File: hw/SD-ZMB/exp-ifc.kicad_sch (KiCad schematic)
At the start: 77 parts, among them J10 HDR 1x04 Socket, J12 SOCKET 02x40 (BRD-CONN), J14 HDR 1x04 Socket, J16 HDR 1x3 Pin, J17 HDR 2x10 Pin, J18 DE9 Male (PINS), J3 HDR 1x02 Pin, J4 BARREL JACK, J8 HDR 02x20 PIN (Ribbon Socket), J9 HDR 02x20 PIN (Ribbon Socket), M1 AES-FTDI_FT234XF_USB_UART_Mod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, M2 DISPLAY, Q1 DMG2305UX, SW2 SW Toggle PCB, U31 3.6864MHz Can Osc, U33 Z84C30 CTC, U34 74ACT10, U35 Z84C42 SIO/2, U36 SN74LVC8T245NS, U37 74AHCT1G02, U39 74AHCT04, U4 74AHCT08, U43 74LVC125AS, U45 WS-RP2040-Zero, U46 MAX232/ST232, U47 74LVC1G06W, U5 74AHCT08

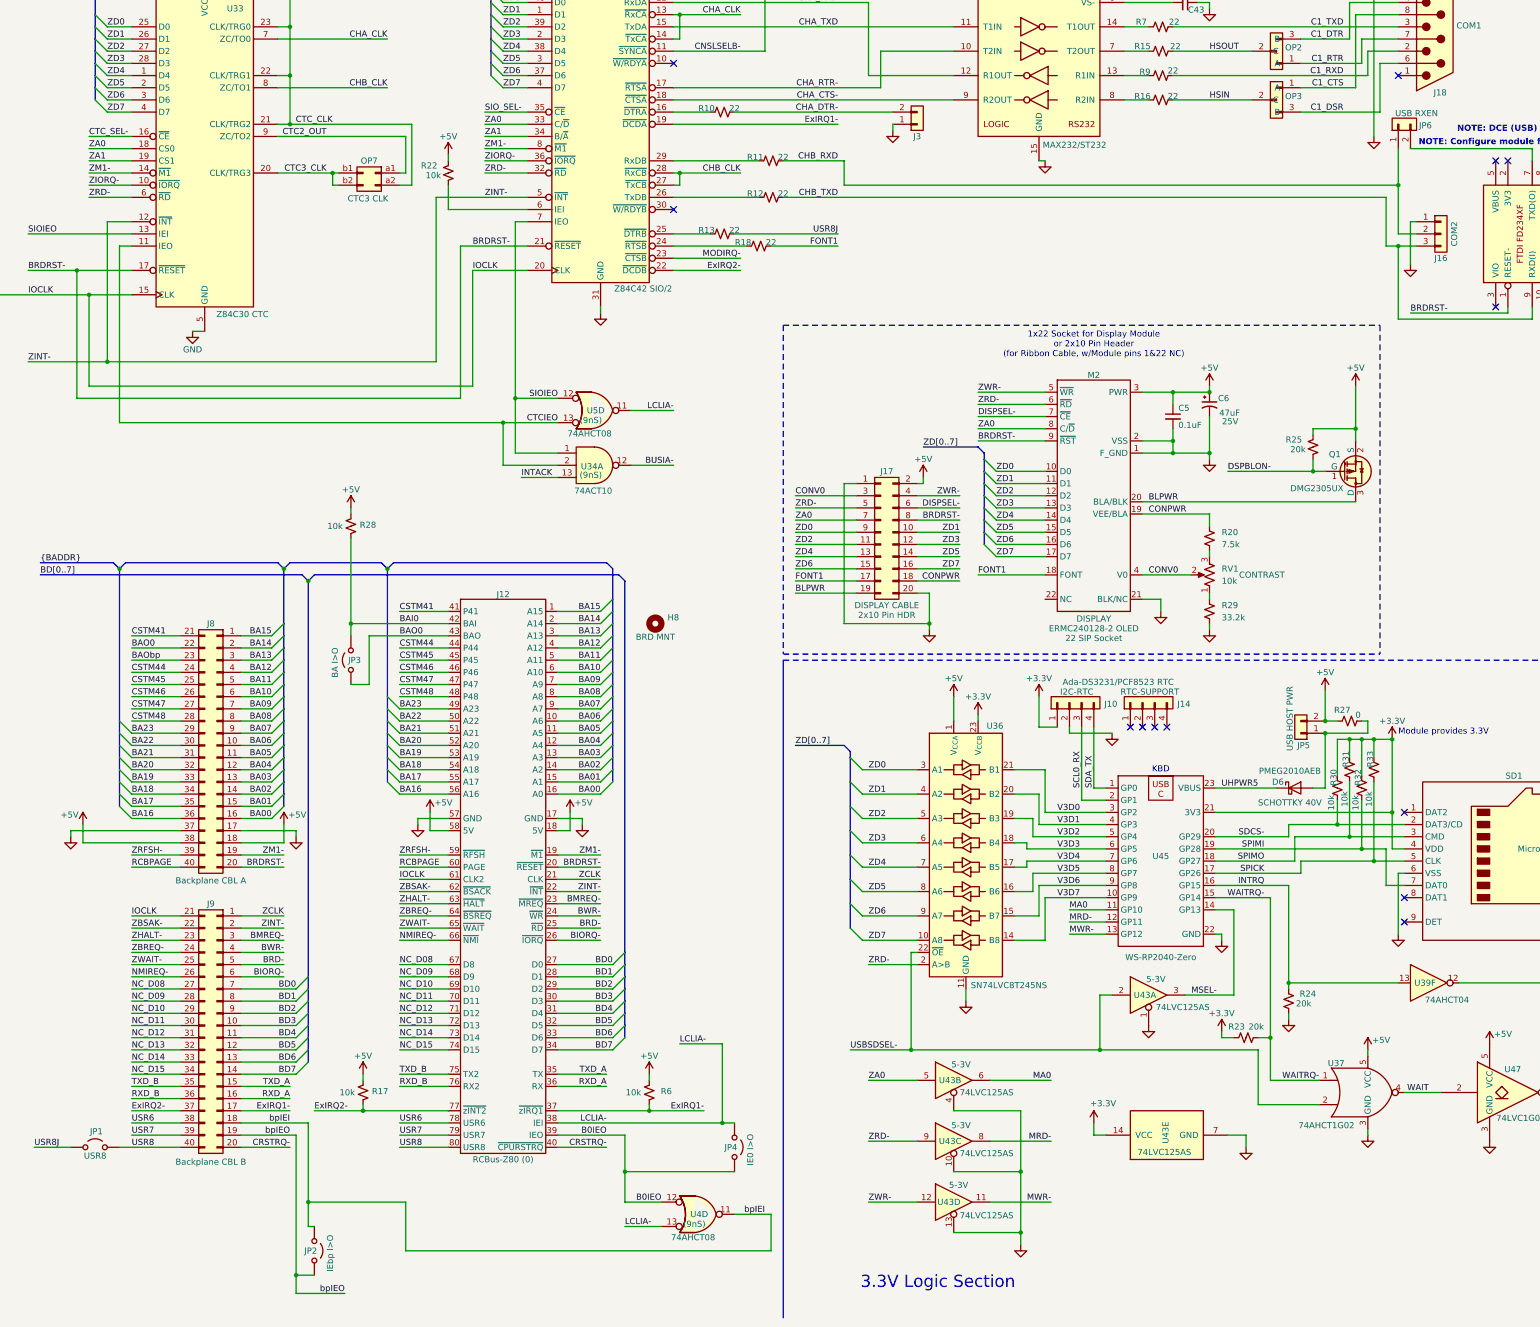
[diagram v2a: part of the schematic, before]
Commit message: ZMB gerbers created. OLED display portion updates.
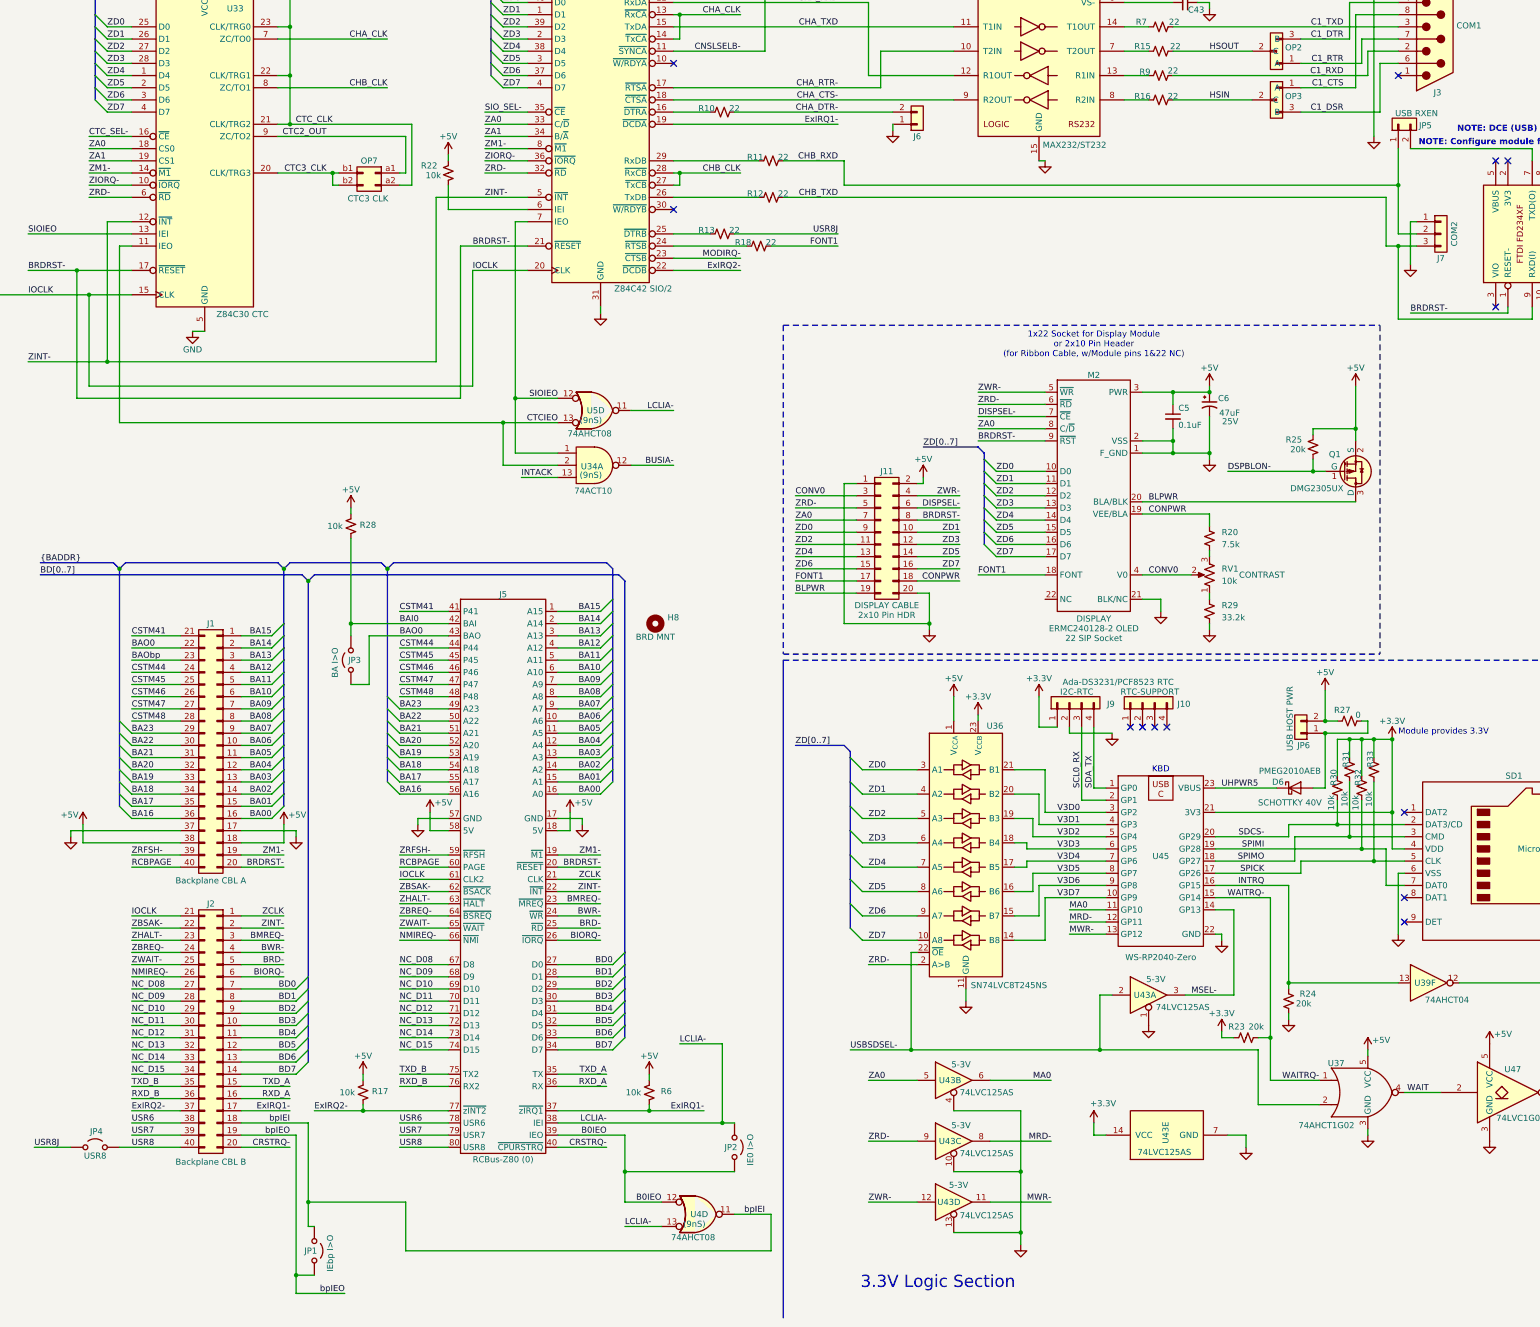
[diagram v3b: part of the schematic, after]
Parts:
- renumbered J8 to J1, J14 to J10, J17 to J11, J9 to J2, J18 to J3, J12 to J5, J3 to J6, J16 to J7, J10 to J9, JP2 to JP1, JP4 to JP2, JP1 to JP4, JP6 to JP5, JP5 to JP6
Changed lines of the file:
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@@
 		(on_board yes)
 		(dnp no)
-		(property "Reference" "JP1"
+		(property "Reference" "JP4"
 			(at 90.424 272.288 0)
 			(effects
@@
 			(project ""
 				(path "/62236e9f-ef27-467c-852b-587c32c473f1/c744ff77-26bb-4e1e-8dbf-a9eea5814d68"
-					(reference "JP1")
+					(reference "JP4")
 					(unit 1)
 				)
@@
 		(on_board yes)
 		(dnp no)
-		(property "Reference" "J8"
+		(property "Reference" "J1"
 			(at 114.3 166.37 0)
 			(effects
@@
 			(project ""
 				(path "/62236e9f-ef27-467c-852b-587c32c473f1/c744ff77-26bb-4e1e-8dbf-a9eea5814d68"
-					(reference "J8")
+					(reference "J1")
 					(unit 1)
 				)
@@
 		(on_board yes)
 		(dnp no)
-		(property "Reference" "J16"
+		(property "Reference" "J7"
 			(at 370.84 90.17 0)
 			(effects
@@
 			(project "SD-ZMB"
 				(path "/62236e9f-ef27-467c-852b-587c32c473f1/c744ff77-26bb-4e1e-8dbf-a9eea5814d68"
-					(reference "J16")
+					(reference "J7")
 					(unit 1)
 				)
@@
 		(on_board yes)
 		(dnp no)
-		(property "Reference" "J14"
+		(property "Reference" "J10"
 			(at 317.246 183.134 90)
 			(effects
@@
 			(project "SD-ZMB"
 				(path "/62236e9f-ef27-467c-852b-587c32c473f1/c744ff77-26bb-4e1e-8dbf-a9eea5814d68"
-					(reference "J14")
+					(reference "J10")
 					(unit 1)
 				)
@@
 		(on_board yes)
 		(dnp no)
-		(property "Reference" "JP6"
+		(property "Reference" "JP5"
 			(at 366.268 62.484 90)
 			(effects
@@
 			(project "SD-ZMB"
 				(path "/62236e9f-ef27-467c-852b-587c32c473f1/c744ff77-26bb-4e1e-8dbf-a9eea5814d68"
-					(reference "JP6")
+					(reference "JP5")
 					(unit 1)
 				)
@@
 		(on_board yes)
 		(dnp no)
-		(property "Reference" "J18"
+		(property "Reference" "J3"
 			(at 369.316 55.626 0)
 			(effects
@@
 			(project ""
 				(path "/62236e9f-ef27-467c-852b-587c32c473f1/c744ff77-26bb-4e1e-8dbf-a9eea5814d68"
-					(reference "J18")
+					(reference "J3")
 					(unit 1)
 				)
@@
 		(on_board yes)
 		(dnp no)
-		(property "Reference" "JP5"
+		(property "Reference" "JP6"
 			(at 340.868 191.77 0)
 			(effects
@@
 			(project "SD-ZMB"
 				(path "/62236e9f-ef27-467c-852b-587c32c473f1/c744ff77-26bb-4e1e-8dbf-a9eea5814d68"
-					(reference "JP5")
+					(reference "JP6")
 					(unit 1)
 				)
@@
 		(on_board yes)
 		(dnp no)
-		(property "Reference" "J10"
+		(property "Reference" "J9"
 			(at 302.006 183.134 90)
 			(effects
@@
 			(project "SD-ZMB"
 				(path "/62236e9f-ef27-467c-852b-587c32c473f1/c744ff77-26bb-4e1e-8dbf-a9eea5814d68"
-					(reference "J10")
+					(reference "J9")
 					(unit 1)
 				)
@@
 		(on_board yes)
 		(dnp no)
-		(property "Reference" "JP2"
+		(property "Reference" "JP1"
 			(at 135.128 297.18 90)
 			(effects
@@
 			(project "SD-ZMB"
 				(path "/62236e9f-ef27-467c-852b-587c32c473f1/c744ff77-26bb-4e1e-8dbf-a9eea5814d68"
-					(reference "JP2")
+					(reference "JP1")
 					(unit 1)
 				)
@@
 		(on_board yes)
 		(dnp no)
-		(property "Reference" "JP4"
+		(property "Reference" "JP2"
 			(at 222.758 275.59 90)
 			(effects
@@
 			(project "SD-ZMB"
 				(path "/62236e9f-ef27-467c-852b-587c32c473f1/c744ff77-26bb-4e1e-8dbf-a9eea5814d68"
-					(reference "JP4")
+					(reference "JP2")
 					(unit 1)
 				)
@@
 		(on_board yes)
 		(dnp no)
-		(property "Reference" "J12"
+		(property "Reference" "J5"
 			(at 175.26 160.274 0)
 			(effects
@@
 			(project ""
 				(path "/62236e9f-ef27-467c-852b-587c32c473f1/c744ff77-26bb-4e1e-8dbf-a9eea5814d68"
-					(reference "J12")
+					(reference "J5")
 					(unit 1)
 				)
@@
 		(on_board yes)
 		(dnp no)
-		(property "Reference" "J3"
+		(property "Reference" "J6"
 			(at 261.62 64.77 0)
 			(effects
@@
 			(project ""
 				(path "/62236e9f-ef27-467c-852b-587c32c473f1/c744ff77-26bb-4e1e-8dbf-a9eea5814d68"
-					(reference "J3")
+					(reference "J6")
 					(unit 1)
 				)
@@
 		(on_board yes)
 		(dnp no)
-		(property "Reference" "J9"
+		(property "Reference" "J2"
 			(at 114.3 224.79 0)
 			(effects
@@
 			(project "SD-ZMB"
 				(path "/62236e9f-ef27-467c-852b-587c32c473f1/c744ff77-26bb-4e1e-8dbf-a9eea5814d68"
-					(reference "J9")
+					(reference "J2")
 					(unit 1)
 				)
@@
 		(on_board yes)
 		(dnp no)
-		(property "Reference" "J17"
+		(property "Reference" "J11"
 			(at 255.27 134.62 0)
 			(effects
@@
 			(project ""
 				(path "/62236e9f-ef27-467c-852b-587c32c473f1/c744ff77-26bb-4e1e-8dbf-a9eea5814d68"
-					(reference "J17")
+					(reference "J11")
 					(unit 1)
 				)

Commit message: PCB received
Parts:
- M2: renamed from U45; Function (none) -> USB KBD
- renumbered C39 to C44, C38 to C45, C44 to C46, M2 to DISP1, U31 to U1, U5 to U15, U4 to U17, U35 to U22, U33 to U26, U47 to U33, U43 to U37, U39 to U41, U37 to U43, U34 to U7, U46 to U8
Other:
- note removed: "KBD"
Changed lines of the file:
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@@
 		)
 	)
-	(text "KBD"
-		(exclude_from_sim no)
-		(at 312.42 196.85 0)
-		(effects
-			(font
-				(size 1.27 1.27)
-				(color 0 0 0 1)
-			)
-		)
-	)
 	(junction
 		(at 361.95 87.63)
@@
 		(on_board yes)
 		(dnp no)
-		(property "Reference" "U43"
+		(property "Reference" "U37"
 			(at 268.478 274.32 0)
 			(effects
@@
 			(project "SD-ZMB"
 				(path "/62236e9f-ef27-467c-852b-587c32c473f1/c744ff77-26bb-4e1e-8dbf-a9eea5814d68"
-					(reference "U43")
+					(reference "U37")
 					(unit 3)
 				)
@@
 		(on_board yes)
 		(dnp no)
-		(property "Reference" "U35"
+		(property "Reference" "U22"
 			(at 201.93 33.02 0)
 			(effects
@@
 			(project ""
 				(path "/62236e9f-ef27-467c-852b-587c32c473f1/c744ff77-26bb-4e1e-8dbf-a9eea5814d68"
-					(reference "U35")
+					(reference "U22")
 					(unit 1)
 				)
@@
 		(on_board yes)
 		(dnp no)
-		(property "Reference" "U33"
-			(at 119.38 38.1 0)
+		(property "Reference" "U26"
+			(at 116.586 34.29 0)
 			(effects
 				(font
@@
 			(project ""
 				(path "/62236e9f-ef27-467c-852b-587c32c473f1/c744ff77-26bb-4e1e-8dbf-a9eea5814d68"
-					(reference "U33")
+					(reference "U26")
 					(unit 1)
 				)
@@
 		(on_board yes)
 		(dnp no)
-		(property "Reference" "U46"
+		(property "Reference" "U8"
 			(at 288.036 22.86 0)
 			(effects
@@
 			(project ""
 				(path "/62236e9f-ef27-467c-852b-587c32c473f1/c744ff77-26bb-4e1e-8dbf-a9eea5814d68"
-					(reference "U46")
+					(reference "U8")
 					(unit 1)
 				)
@@
 		(on_board yes)
 		(dnp no)
-		(property "Reference" "M2"
+		(property "Reference" "DISP1"
 			(at 298.45 114.554 0)
 			(effects
@@
 			(project ""
 				(path "/62236e9f-ef27-467c-852b-587c32c473f1/c744ff77-26bb-4e1e-8dbf-a9eea5814d68"
-					(reference "M2")
+					(reference "DISP1")
 					(unit 1)
 				)
@@
 		(on_board yes)
 		(dnp no)
-		(property "Reference" "U34"
+		(property "Reference" "U7"
 			(at 193.802 133.604 0)
 			(effects
@@
 			(project "SD-ZMB"
 				(path "/62236e9f-ef27-467c-852b-587c32c473f1/c744ff77-26bb-4e1e-8dbf-a9eea5814d68"
-					(reference "U34")
+					(reference "U7")
 					(unit 1)
 				)
@@
 		(on_board yes)
 		(dnp no)
-		(property "Reference" "U39"
+		(property "Reference" "U41"
 			(at 367.538 241.3 0)
 			(effects
@@
 			(project "SD-ZMB"
 				(path "/62236e9f-ef27-467c-852b-587c32c473f1/c744ff77-26bb-4e1e-8dbf-a9eea5814d68"
-					(reference "U39")
+					(reference "U41")
 					(unit 6)
 				)
@@
 		(on_board yes)
 		(dnp no)
-		(property "Reference" "C44"
+		(property "Reference" "C46"
 			(at 41.656 130.556 90)
 			(effects
@@
 			(project "SD-ZMB"
 				(path "/62236e9f-ef27-467c-852b-587c32c473f1/c744ff77-26bb-4e1e-8dbf-a9eea5814d68"
-					(reference "C44")
+					(reference "C46")
 					(unit 1)
 				)
@@
 		(on_board yes)
 		(dnp no)
-		(property "Reference" "C38"
+		(property "Reference" "C45"
 			(at 267.716 28.194 90)
 			(effects
@@
 			(project "SD-ZMB"
 				(path "/62236e9f-ef27-467c-852b-587c32c473f1/c744ff77-26bb-4e1e-8dbf-a9eea5814d68"
-					(reference "C38")
+					(reference "C45")
 					(unit 1)
 				)
@@
 		(on_board yes)
 		(dnp no)
-		(property "Reference" "U4"
+		(property "Reference" "U17"
 			(at 216.154 289.56 0)
 			(effects
@@
 			(project "SD-ZMB"
 				(path "/62236e9f-ef27-467c-852b-587c32c473f1/c744ff77-26bb-4e1e-8dbf-a9eea5814d68"
-					(reference "U4")
+					(reference "U17")
 					(unit 4)
 				)
@@
 		(on_board yes)
 		(dnp no)
-		(property "Reference" "U37"
+		(property "Reference" "U43"
 			(at 348.996 258.064 0)
 			(effects
@@
 			(project "SD-ZMB"
 				(path "/62236e9f-ef27-467c-852b-587c32c473f1/c744ff77-26bb-4e1e-8dbf-a9eea5814d68"
-					(reference "U37")
+					(reference "U43")
 					(unit 1)
 				)
@@
 		(on_board yes)
 		(dnp no)
-		(property "Reference" "U31"
+		(property "Reference" "U1"
 			(at 32.004 33.274 0)
 			(effects
@@
 			(project "SD-ZMB"
 				(path "/62236e9f-ef27-467c-852b-587c32c473f1/c744ff77-26bb-4e1e-8dbf-a9eea5814d68"
-					(reference "U31")
+					(reference "U1")
 					(unit 1)
 				)
@@
 		(on_board yes)
 		(dnp no)
-		(property "Reference" "C39"
+		(property "Reference" "C44"
 			(at 280.416 19.304 90)
 			(effects
@@
 			(project "SD-ZMB"
 				(path "/62236e9f-ef27-467c-852b-587c32c473f1/c744ff77-26bb-4e1e-8dbf-a9eea5814d68"
-					(reference "C39")
+					(reference "C44")
 					(unit 1)
 				)
@@
 		(on_board yes)
 		(dnp no)
-		(property "Reference" "U43"
+		(property "Reference" "U37"
 			(at 313.436 274.828 0)
 			(effects
@@
 			(project "SD-ZMB"
 				(path "/62236e9f-ef27-467c-852b-587c32c473f1/c744ff77-26bb-4e1e-8dbf-a9eea5814d68"
-					(reference "U43")
+					(reference "U37")
 					(unit 5)
 				)
@@
 		(on_board yes)
 		(dnp no)
-		(property "Reference" "U45"
+		(property "Reference" "M2"
 			(at 312.42 214.884 0)
 			(effects
@@
 			)
 		)
-		(property "CPU" ""
-			(at 312.42 214.63 0)
-			(effects
-				(font
-					(size 1.27 1.27)
-				)
-				(hide yes)
-			)
-		)
-		(property "OPT-A" ""
-			(at 312.42 214.63 0)
-			(effects
-				(font
-					(size 1.27 1.27)
-				)
-				(hide yes)
-			)
-		)
-		(property "OPT-B" ""
-			(at 312.42 214.63 0)
+		(property "Function" "USB KBD"
+			(at 312.42 196.342 0)
 			(effects
 				(font
 					(size 1.27 1.27)
 				)
-				(hide yes)
 			)
 		)
@@
 			(project ""
 				(path "/62236e9f-ef27-467c-852b-587c32c473f1/c744ff77-26bb-4e1e-8dbf-a9eea5814d68"
-					(reference "U45")
+					(reference "M2")
 					(unit 1)
 				)
@@
 		(on_board yes)
 		(dnp no)
-		(property "Reference" "U43"
+		(property "Reference" "U37"
 			(at 268.478 261.62 0)
 			(effects
@@
 			(project "SD-ZMB"
 				(path "/62236e9f-ef27-467c-852b-587c32c473f1/c744ff77-26bb-4e1e-8dbf-a9eea5814d68"
-					(reference "U43")
+					(reference "U37")
 					(unit 2)
 				)
@@
 		(on_board yes)
 		(dnp no)
-		(property "Reference" "U43"
+		(property "Reference" "U37"
 			(at 268.224 287.02 0)
 			(effects
@@
 			(project "SD-ZMB"
 				(path "/62236e9f-ef27-467c-852b-587c32c473f1/c744ff77-26bb-4e1e-8dbf-a9eea5814d68"
-					(reference "U43")
+					(reference "U37")
 					(unit 4)
 				)
@@
 		(on_board yes)
 		(dnp no)
-		(property "Reference" "U43"
+		(property "Reference" "U37"
 			(at 309.118 243.84 0)
 			(effects
@@
 			(project "SD-ZMB"
 				(path "/62236e9f-ef27-467c-852b-587c32c473f1/c744ff77-26bb-4e1e-8dbf-a9eea5814d68"
-					(reference "U43")
+					(reference "U37")
 					(unit 1)
 				)
@@
 		(on_board yes)
 		(dnp no)
-		(property "Reference" "U47"
+		(property "Reference" "U33"
 			(at 385.826 259.334 0)
 			(effects
@@
 			(project ""
 				(path "/62236e9f-ef27-467c-852b-587c32c473f1/c744ff77-26bb-4e1e-8dbf-a9eea5814d68"
-					(reference "U47")
+					(reference "U33")
 					(unit 1)
 				)
@@
 		(on_board yes)
 		(dnp no)
-		(property "Reference" "U5"
+		(property "Reference" "U15"
 			(at 194.564 121.92 0)
 			(effects
@@
 			(project "SD-ZMB"
 				(path "/62236e9f-ef27-467c-852b-587c32c473f1/c744ff77-26bb-4e1e-8dbf-a9eea5814d68"
-					(reference "U5")
+					(reference "U15")
 					(unit 4)
 				)
